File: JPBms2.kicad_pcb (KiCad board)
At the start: 4 copper layers, 69 x 39 mm, 134 parts, among them J1 XT30PW-M, J2 Conn_ARM_SWD_TagConnect_TC2030, Q1 AO3400A, Q10 2N7002, Q11 SK2301AW, Q12 SK2301AW, Q13 2N7002, Q14 SK2301AW, Q15 SK2301AW, Q16 2N7002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

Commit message: 94 unrouted
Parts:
- moved C7 10.3 mm to (125.6, 81.8), turned to -90 degrees
- moved R55 4.07 mm to (146.3, 71.4), turned to 180 degrees
- moved C22 4.07 mm to (129.0, 82.3), turned to -90 degrees
- moved R56 4.06 mm to (146.3, 75.4), turned to 180 degrees
- moved R4 3.51 mm to (124.1, 81.8), turned to 90 degrees
- moved R7 3.30 mm to (132.1, 82.3), turned to 90 degrees
- moved U1 3.07 mm to (147.8, 87.6), turned to 0 degrees
- moved D3 2.93 mm to (129.7, 79.0)
- moved R1 2.78 mm to (140.3, 78.5)
- moved C17 2.77 mm to (137.5, 78.2), turned to 90 degrees
- moved D18 2.54 mm to (132.3, 79.0)
- moved R32 2.42 mm to (138.8, 77.6), turned to 90 degrees
- moved C1 2.16 mm to (145.2, 87.7), turned to -90 degrees
- moved R36 2.09 mm to (140.2, 84.8)
- moved R37 1.99 mm to (140.2, 83.3)
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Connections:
- U3 pad 14: VBATT_ADC -> VSOLAR_ADC
- U3 pad 15: VSOLAR_ADC -> VBATT_ADC
- U3 pad 21: VBATT_ADC_EN -> CELL4V_ADC_EN
- U3 pad 23: CELL4V_ADC_EN -> VBATT_ADC_EN
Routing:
- net VDD: track 25.4 -> 76.6 mm, vias 0 -> 4
- net Net-(U1-OUT): track 0.00 -> 40.1 mm, vias 0 -> 2
- net /BuckBoost/DRIVER_VCC: track 9.47 -> 49.0 mm, vias 0 -> 2
- net CELL_8V: track 20.8 -> 59.7 mm, vias 0 -> 2
- net CELL_4V: track 23.4 -> 59.5 mm, vias 0 -> 2
- net Net-(Q12-D): track 0.00 -> 33.3 mm
- net VSOLAR: track 10.7 -> 34.6 mm
- net /MCU/USART1_RX: track 1.42 -> 18.0 mm
- net GND: track 9.99 -> 25.8 mm, vias 0 -> 15
- net +BATT: track 66.8 -> 79.2 mm
- net Net-(Q11-G): track 0.00 -> 12.0 mm
- net Net-(Q17-G): track 0.00 -> 10.5 mm
- net Net-(Q14-G): track 0.00 -> 10.5 mm
- net VBATT_ADC: track 2.80 -> 11.6 mm
- net /MCU/SWITCH: track 0.00 -> 8.33 mm
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- added copper zone on F.Cu, net /BuckBoost/VS_A

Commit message: 35 left
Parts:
- moved R36 11.3 mm to (129.2, 87.0), turned to 180 degrees
- moved R37 11.3 mm to (129.2, 85.5)
- moved C12 0.35 mm to (133.7, 73.2)
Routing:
- net GND: track 25.8 -> 92.0 mm, vias 15 -> 64
- net DD_TOP_B: track 0.00 -> 52.5 mm, vias 0 -> 2
- net DD_BOT_B: track 0.00 -> 49.6 mm, vias 0 -> 2
- net DD_TOP_A: track 0.00 -> 37.7 mm, vias 0 -> 2
- net /MCU/SWITCH: track 8.33 -> 45.4 mm, vias 0 -> 2
- net DD_BOT_A: track 0.00 -> 34.1 mm, vias 0 -> 2
- net /MCU/SWCLK: track 0.00 -> 31.7 mm, vias 0 -> 2
- net COMP2_INP: track 2.66 -> 32.4 mm, vias 0 -> 2
- net /MCU/SWDIO: track 0.00 -> 24.3 mm, vias 0 -> 2
- net VBATT_ADC_EN: track 0.00 -> 17.0 mm
- net VDD: track 76.6 -> 93.6 mm
- net CELL4V_ADC_EN: track 0.00 -> 11.8 mm, vias 0 -> 2
- net /MCU/NRST: track 2.19 -> 12.2 mm, vias 0 -> 1
- net /BuckBoost/VS_A: track 7.00 -> 16.0 mm
- net CELL8V_ADC_EN: track 0.00 -> 8.58 mm, vias 0 -> 2
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
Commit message: 17 left
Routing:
- net +BATT: track 79.2 -> 134.8 mm, vias 0 -> 3
- net NBAL_1: track 0.00 -> 36.6 mm, vias 0 -> 4
- net /MCU/LED_ERROR: track 0.00 -> 35.6 mm, vias 0 -> 2
- net /MCU/LED_ON: track 0.00 -> 35.2 mm
- net /MCU/LED_ACTIVE: track 0.00 -> 35.1 mm, vias 0 -> 2
- net DRIVERS_EN: track 2.08 -> 36.9 mm, vias 1 -> 2
- net /MCU/NRST: track 12.2 -> 38.0 mm, vias 1 -> 4
- net NBAL_2: track 0.00 -> 15.2 mm, vias 0 -> 3
- net Net-(Q17-D): track 0.00 -> 8.42 mm
- net Net-(Q14-D): track 0.00 -> 8.39 mm
- net Net-(Q11-D): track 0.00 -> 8.24 mm
- net NBAL_3: track 0.00 -> 8.13 mm, vias 0 -> 2
- net GND: track 92.0 -> 96.6 mm, vias 64 -> 74
- net /BuckBoost/VS_A: track 16.0 -> 19.5 mm
- net DD_BOT_A: track 34.1 -> 35.9 mm
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
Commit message: It is routed
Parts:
- turned D11 to 180 degrees
- turned D12 to 180 degrees
- turned D13 to 180 degrees
- turned R43 to 180 degrees
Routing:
- net Net-(D11-A): track 4.87 -> 25.9 mm, vias 0 -> 2
- net Net-(D12-A): track 4.17 -> 22.8 mm, vias 0 -> 2
- net CELL_8V: track 59.8 -> 73.1 mm, vias 2 -> 4
- net Net-(D13-A): track 4.79 -> 17.2 mm, vias 0 -> 2
- net CELL_4V: track 60.5 -> 70.4 mm, vias 2 -> 4
- net Net-(U1-OUT): track 40.1 -> 48.1 mm, vias 2 -> 4
- net GND: track 96.6 -> 104.2 mm, vias 74 -> 112
- net Net-(D12-K): track 0.00 -> 1.24 mm
- net Net-(D13-K): track 0.00 -> 1.24 mm
- net DD_BOT_B: track 49.8 -> 51.0 mm
- net Net-(D11-K): track 0.00 -> 1.24 mm
- net Net-(U4-LVG): track 9.50 -> 8.64 mm
- net /MCU/LED_ERROR: track 35.6 -> 36.4 mm
- net +BATT: track 134.8 -> 133.9 mm
- net NBAL_2: track 15.2 -> 14.9 mm, vias 3 -> 2

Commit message: Fine tuning routing
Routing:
- net /MCU/SWITCH: track 45.7 -> 48.6 mm
- net VBATT_ADC_EN: track 17.0 -> 19.3 mm
- net /BuckBoost/DRIVER_VCC: track 50.0 -> 51.7 mm
- net DD_BOT_B: track 51.0 -> 49.8 mm
- net DD_TOP_B: track 53.1 -> 53.8 mm
- net GND: vias 112 -> 113
- net /BuckBoost/VS_B: vias 0 -> 11
- net /BuckBoost/VS_A: vias 0 -> 9
- added copper zone on F.Cu, net +BATT
- added copper zone on B.Cu, net /BuckBoost/VS_A
- added copper zone on B.Cu, net /BuckBoost/VS_B
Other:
- board text added: "V1.2 X Move solar adc line to other layer for less noise? X Move adc sampling capacitors closest to stm32 X stm power pins should be wired to capacitors, then those wired to vcc/gnd - multiple gnd vias around decoupling caps X balance resistors are placed in a weird grouping X bootstrap diodes backwards X Check, do I need vcc for level shifting on the BMP uart? X Could I make the uart only turn o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"
- board text removed: "V1.2 - Move solar adc line to other layer for less noise? - Move adc sampling capacitors closest to stm32 - stm power pins should be wired to capacitors, then those wired to vcc/gnd - multiple gnd vias around decoupling caps X balance resistors are placed in a weird grouping X bootstrap diodes backwards X Check, do I need vcc for level shifting on the BMP uart? X Could I make the uart only turn o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"

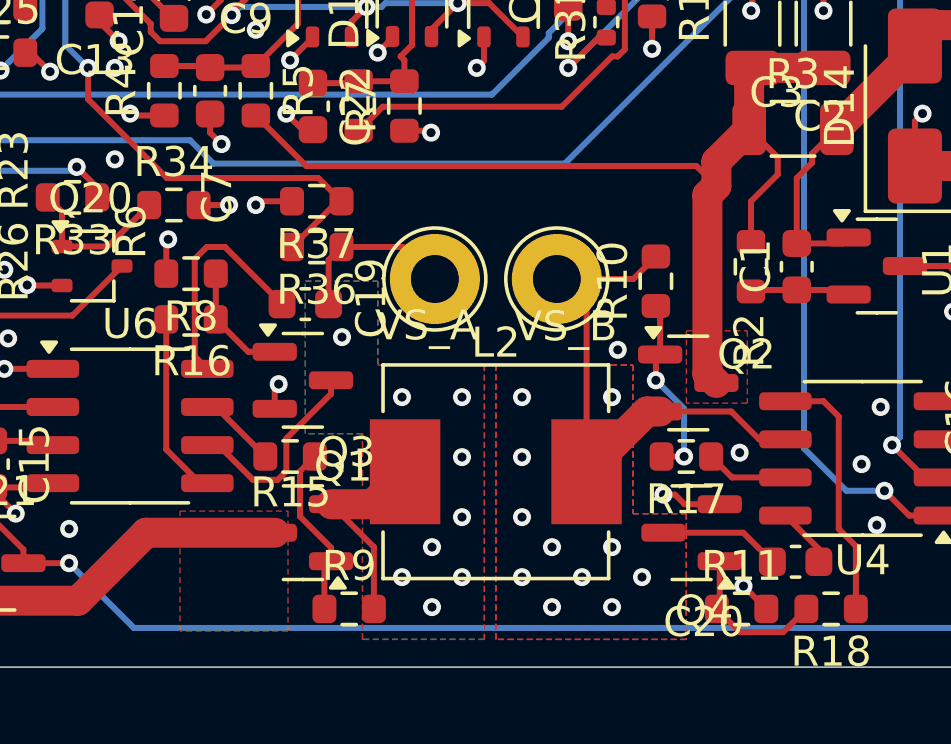
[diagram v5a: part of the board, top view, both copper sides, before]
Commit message: Better thermal pads
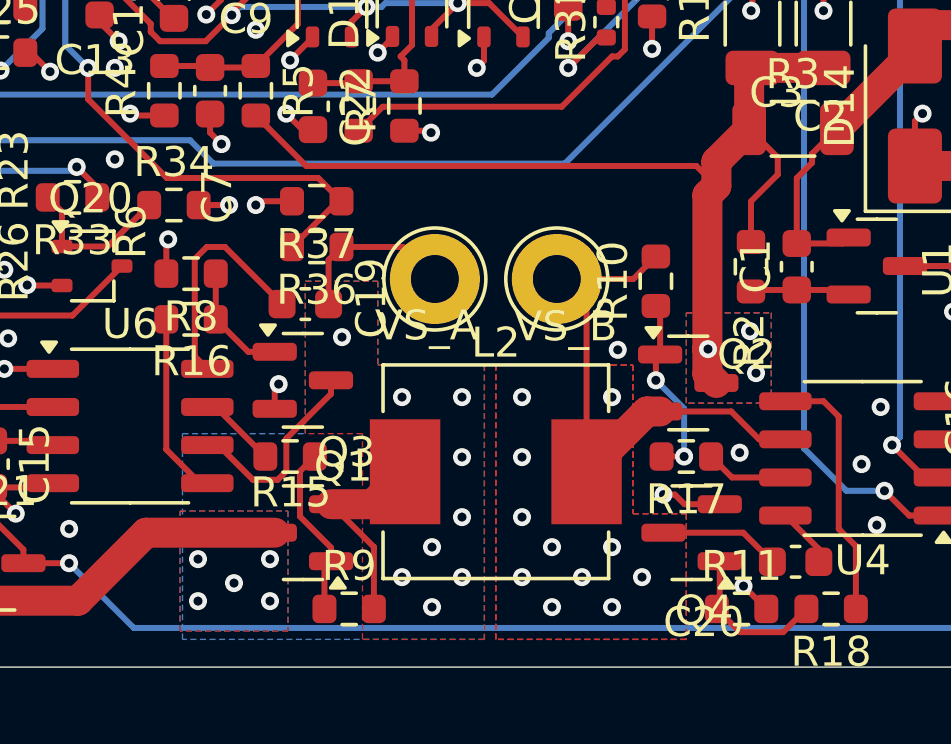
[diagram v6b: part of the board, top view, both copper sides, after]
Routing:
- net VSOLAR: vias 0 -> 3
- net +BATT: vias 3 -> 8
- added copper zone on B.Cu, net +BATT
- added copper zone on B.Cu, net VSOLAR
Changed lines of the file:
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@@
 	)
 	(via
+		(at 127.6 97.4)
+		(size 0.6)
+		(drill 0.3)
+		(layers "F.Cu" "B.Cu")
+		(free yes)
+		(net 7)
+	)
+	(via
+		(at 127.6 98.8)
+		(size 0.6)
+		(drill 0.3)
+		(layers "F.Cu" "B.Cu")
+		(free yes)
+		(net 7)
+	)
+	(via
+		(at 125.2 97.4)
+		(size 0.6)
+		(drill 0.3)
+		(layers "F.Cu" "B.Cu")
+		(free yes)
+		(net 7)
+	)
+	(via
 		(at 143.764 67.564)
 		(size 0.6)
@@
 	)
 	(via
+		(at 125.2 98.8)
+		(size 0.6)
+		(drill 0.3)
+		(layers "F.Cu" "B.Cu")
+		(free yes)
+		(net 7)
+	)
+	(via
 		(at 139.806555 63.388)
 		(size 0.6)
@@
 	)
 	(via
+		(at 126.4 98.2)
+		(size 0.6)
+		(drill 0.3)
+		(layers "F.Cu" "B.Cu")
+		(free yes)
+		(net 7)
+	)
+	(via
 		(at 140.399002 67.499998)
 		(size 0.6)
@@
 	)
 	(segment
+		(start 142.2 90.4)
+		(end 142.179652 90.379652)
+		(width 1)
+		(layer "F.Cu")
+		(net 13)
+	)
+	(segment
+		(start 142.179652 90.420348)
+		(end 142.2 90.4)
+		(width 1)
+		(layer "F.Cu")
+		(net 13)
+	)
+	(segment
 		(start 144.526 84.582)
 		(end 143.632783 85.475217)
@@
 	)
 	(segment
-		(start 142.179652 91.229351)
+		(start 142.179652 90.379652)
 		(end 142.179652 85.262999)
 		(width 1)
@@
 	)
 	(segment
+		(start 142.179652 91.229351)
+		(end 142.179652 90.420348)
+		(width 1)
+		(layer "F.Cu")
+		(net 13)
+	)
+	(segment
 		(start 142.479651 91.52935)
 		(end 142.179652 91.229351)
@@
 		(net 13)
 	)
+	(via
+		(at 143.8 91.2)
+		(size 0.6)
+		(drill 0.3)
+		(layers "F.Cu" "B.Cu")
+		(free yes)
+		(net 13)
+	)
+	(via
+		(at 142.2 90.4)
+		(size 0.6)
+		(drill 0.3)
+		(layers "F.Cu" "B.Cu")
+		(net 13)
+	)
+	(via
+		(at 143.6 89.8)
+		(size 0.6)
+		(drill 0.3)
+		(layers "F.Cu" "B.Cu")
+		(free yes)
+		(net 13)
+	)
 	(segment
 		(start 122.750924 70.07)
@@
 	)
 	(zone
-		(net 13)
-		(net_name "VSOLAR")
+		(net 22)
+		(net_name "/BuckBoost/VS_B")
 		(layer "F.Cu")
 		(hatch edge 0.5)
-		(priority 2)
+		(priority 3)
 		(connect_pads yes
 			(clearance 0.2)
@@
 		(polygon
 			(pts
-				(xy 141.478 89.789) (xy 143.51 89.789) (xy 143.51 92.202) (xy 141.478 92.202)
+				(xy 135.128 90.932) (xy 139.7 90.932) (xy 139.7 95.885) (xy 141.478 95.885) (xy 141.478 100.076)
+				(xy 135.128 100.076)
 			)
 		)
 	)
 	(zone
-		(net 22)
-		(net_name "/BuckBoost/VS_B")
+		(net 20)
+		(net_name "/BuckBoost/VS_A")
 		(layer "F.Cu")
 		(hatch edge 0.5)
-		(priority 3)
+		(priority 4)
 		(connect_pads yes
 			(clearance 0.2)
@@
 		(polygon
 			(pts
-				(xy 135.128 90.932) (xy 139.7 90.932) (xy 139.7 95.885) (xy 141.478 95.885) (xy 141.478 100.076)
-				(xy 135.128 100.076)
+				(xy 128.778 88.138) (xy 131.191 88.138) (xy 131.191 90.932) (xy 134.747 90.932) (xy 134.747 100.076)
+				(xy 130.683 100.076) (xy 130.683 93.218) (xy 128.778 93.218)
 			)
 		)
 	)
 	(zone
-		(net 7)
-		(net_name "+BATT")
-		(layer "F.Cu")
+		(net 13)
+		(net_name "VSOLAR")
+		(layers "F&B.Cu")
 		(hatch edge 0.5)
-		(priority 5)
+		(priority 2)
 		(connect_pads yes
 			(clearance 0.2)
@@
 			(thermal_gap 0.5)
 			(thermal_bridge_width 0.5)
+			(island_removal_mode 1)
+			(island_area_min 10)
 		)
 		(polygon
 			(pts
-				(xy 124.6 95.8) (xy 128.2 95.8) (xy 128.2 99.8) (xy 124.6 99.8)
+				(xy 141.478 89.189) (xy 144.31 89.189) (xy 144.31 92.202) (xy 141.478 92.202)
 			)
 		)
 	)
 	(zone
-		(net 20)
-		(net_name "/BuckBoost/VS_A")
-		(layer "F.Cu")
+		(net 7)
+		(net_name "+BATT")
+		(layers "F&B.Cu")
 		(hatch edge 0.5)
-		(priority 4)
+		(priority 5)
 		(connect_pads yes
 			(clearance 0.2)
@@
 			(thermal_gap 0.5)
 			(thermal_bridge_width 0.5)
+			(island_removal_mode 1)
+			(island_area_min 10)
 		)
 		(polygon
 			(pts
-				(xy 128.778 88.138) (xy 131.191 88.138) (xy 131.191 90.932) (xy 134.747 90.932) (xy 134.747 100.076)
-				(xy 130.683 100.076) (xy 130.683 93.218) (xy 128.778 93.218)
+				(xy 124.6 95.8) (xy 128.2 95.8) (xy 128.2 99.8) (xy 124.6 99.8)
 			)
 		)
@@
 			(pts
 				(xy 128.778 88.138) (xy 131.191 88.138) (xy 131.191 90.932) (xy 134.747 90.932) (xy 134.747 100.076)
-				(xy 130.683 100.076) (xy 130.683 93.218) (xy 128.778 93.218)
+				(xy 124.683 100.076) (xy 124.683 93.218) (xy 128.778 93.218)
 			)
 		)

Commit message: Starting cleanup
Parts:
- renumbered L2 to L1
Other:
- board text removed: "2.5V"
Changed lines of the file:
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@@
 		(tags "SO SO")
 		(property "Reference" "U4"
-			(at 0 -3.4 180)
+			(at -4.645 -2.157 180)
 			(layer "F.SilkS")
 			(effects
@@
 		(tags "resistor")
 		(property "Reference" "R9"
-			(at 0 -1.43 0)
+			(at 0 1.34 0)
 			(layer "F.SilkS")
 			(effects
@@
 		(tags "capacitor")
 		(property "Reference" "C19"
-			(at -2.2 0.2 -90)
+			(at -2.022 0.1 -90)
 			(layer "F.SilkS")
 			(effects
@@
 		(tags "LED")
 		(property "Reference" "D12"
-			(at 0 -1.43 180)
+			(at -5.2025 -0.118 180)
 			(layer "F.SilkS")
 			(effects
@@
 		(tags "SOT TO_SOT_SMD")
 		(property "Reference" "U1"
-			(at 2.044175 0.125049 90)
+			(at -0.028 2.37 180)
 			(layer "F.SilkS")
 			(effects
@@
 		(descr "Inductor, Sunlord, MWSA0605S, 7.0x6.6x4.8mm, https://sunlordinc.com/Download.aspx?file=L1VwbG9hZEZpbGVzL1BERl9DYXQvMjAyMjExMTUxNDQ4MDU0NTQucGRm&lan=en")
 		(tags "Inductor mwsa")
-		(property "Reference" "L2"
+		(property "Reference" "L1"
 			(at 0 -4.3 0)
 			(layer "F.SilkS")
@@
 		(tags "fuse")
 		(property "Reference" "F2"
-			(at -3.38 0.28 0)
+			(at 2.911504 0.044 0)
 			(layer "F.SilkS")
 			(effects
@@
 		(tags "resistor")
 		(property "Reference" "R36"
-			(at 0 -1.43 180)
+			(at 2.159 -0.005 -90)
 			(layer "F.SilkS")
 			(effects
@@
 		(tags "capacitor")
 		(property "Reference" "C4"
-			(at 2.75 -0.5 0)
+			(at 1.482 -2.088 0)
 			(layer "F.SilkS")
 			(effects
@@
 		(tags "resistor")
 		(property "Reference" "R15"
-			(at 0.025 1.2 0)
+			(at 1.93 -0.18 90)
 			(layer "F.SilkS")
 			(effects
@@
 			(at 0 -1.17 180)
 			(layer "F.SilkS")
+			(hide yes)
 			(effects
 				(font
@@
 		(tags "capacitor")
 		(property "Reference" "C1"
-			(at -0.017643 1.362286 90)
+			(at -2.453547 -0.041275 90)
 			(layer "F.SilkS")
 			(effects
@@
 		(tags "tag connect programming header pogo pins")
 		(property "Reference" "J2"
-			(at -4.99 2.585 180)
+			(at 0.01 4.485 180)
 			(layer "F.SilkS")
 			(effects
@@
 			(at -0.05 1.8 180)
 			(layer "F.SilkS")
+			(hide yes)
 			(effects
 				(font
@@
 		(tags "resistor")
 		(property "Reference" "R18"
-			(at 0 -1.43 180)
+			(at 0 -1.54 180)
 			(layer "F.SilkS")
 			(effects
@@
 		(tags "Diode SOD882 DFN1006-2")
 		(property "Reference" "D15"
-			(at 0.15 1.8 180)
+			(at 0.834 -2.201864 180)
 			(layer "F.SilkS")
+			(hide yes)
 			(effects
 				(font
@@
 			(at 0 -1.17 180)
 			(layer "F.SilkS")
+			(hide yes)
 			(effects
 				(font
@@
 		(tags "LED")
 		(property "Reference" "D13"
-			(at 0 -1.43 180)
+			(at -5.2025 0.006 180)
 			(layer "F.SilkS")
 			(effects
@@
 			(at -0.05 1.8 180)
 			(layer "F.SilkS")
+			(hide yes)
 			(effects
 				(font
@@
 			(at 0 -1.17 180)
 			(layer "F.SilkS")
+			(hide yes)
 			(effects
 				(font
@@
 		(tags "LED")
 		(property "Reference" "D11"
-			(at 0 -1.43 180)
+			(at -5.2025 -0.042 180)
 			(layer "F.SilkS")
 			(effects
@@
 		(tags "connector Molex PicoBlade side entry")
 		(property "Reference" "UART1"
-			(at 2.968 4.211 0)
+			(at 0.348 -2.436 0)
 			(layer "F.SilkS")
 			(effects
@@
 		(tags "capacitor")
 		(property "Reference" "C11"
-			(at 2.66 0.22 90)
+			(at 2.86 -0.08 90)
 			(layer "F.SilkS")
 			(effects
@@
 		(tags "resistor")
 		(property "Reference" "R37"
-			(at 0 -1.43 180)
+			(at -0.041 1.071 0)
 			(layer "F.SilkS")
 			(effects
@@
 		(tags "capacitor")
 		(property "Reference" "C5"
-			(at 2.848852 0.865192 0)
+			(at 2.848852 -0.138 0)
 			(layer "F.SilkS")
 			(effects
@@
 		(tags "resistor")
 		(property "Reference" "R2"
-			(at 2.455 0.0485 90)
+			(at -2.453547 0.032783 90)
 			(layer "F.SilkS")
 			(effects
@@
 		(tags "capacitor")
 		(property "Reference" "C16"
-			(at -0.025 1.25 90)
+			(at -0.025 -1.508 90)
 			(layer "F.SilkS")
 			(effects
@@
 		(tags "capacitor")
 		(property "Reference" "C20"
-			(at -3.063 2.013 0)
+			(at 2.879475 -0.088936 0)
 			(layer "F.SilkS")
 			(effects
@@
 		(tags "fuse")
 		(property "Reference" "F1"
-			(at -3.28 0.08 0)
+			(at 2.898 0.104 0)
 			(layer "F.SilkS")
 			(effects
@@
 		(tags "capacitor")
 		(property "Reference" "C21"
-			(at 0 1.4 90)
+			(at -1.989125 0.195515 180)
 			(layer "F.SilkS")
 			(effects
@@
 		(tags "Diode SOD882 DFN1006-2")
 		(property "Reference" "D7"
-			(at 0 -1.35 90)
+			(at -0.262 1.456 90)
 			(layer "F.SilkS")
 			(effects
@@
 		(tags "resistor")
 		(property "Reference" "R10"
-			(at 0 -1.43 -90)
+			(at 0 1.338 -90)
 			(layer "F.SilkS")
 			(effects
@@
 		(tags "SOT TO_SOT_SMD")
 		(property "Reference" "Q4"
-			(at -0.4135 -2.6 180)
+			(at 0.8535 -2.48 180)
 			(layer "F.SilkS")
 			(effects
@@
 		(tags "SOT TO_SOT_SMD")
 		(property "Reference" "Q1"
-			(at -1.3375 2.2 180)
+			(at 0.8995 -2.48 0)
 			(layer "F.SilkS")
 			(effects
@@
 		(tags "SOT TO_SOT_SMD")
 		(property "Reference" "Q3"
-			(at 1.445 2.4 0)
+			(at 2.905 -1.24 0)
 			(layer "F.SilkS")
 			(effects
@@
 		(tags "fuse")
 		(property "Reference" "F3"
-			(at -3.38 0.28 0)
+			(at 2.898 -0.016 0)
 			(layer "F.SilkS")
 			(effects
@@
 		(tags "SO SO")
 		(property "Reference" "U6"
-			(at 0 -3.4 0)
+			(at -1.136 -3.364 0)
 			(layer "F.SilkS")
 			(effects
@@
 		(tags "Diode SOD882 DFN1006-2")
 		(property "Reference" "D8"
-			(at 0 -1.35 90)
+			(at 1.96 -0.144 90)
 			(layer "F.SilkS")
 			(effects
@@
 		(tags "resistor")
 		(property "Reference" "R11"
-			(at 0 -1.43 0)
+			(at 0 1.54 0)
 			(layer "F.SilkS")
 			(effects
@@
 		(tags "resistor")
 		(property "Reference" "R17"
-			(at 0 -1.43 180)
+			(at -1.922 -0.02 90)
 			(layer "F.SilkS")
 			(effects
@@
 		(tags "SOT TO_SOT_SMD")
 		(property "Reference" "Q2"
-			(at 1.9375 -0.946 0)
+			(at 3.057849 -0.92935 0)
 			(layer "F.SilkS")
 			(effects
@@
 		)
 	)
-	(gr_text "2.5V"
-		(at 113.2 65.4 0)
-		(layer "F.SilkS")
-		(effects
-			(font
-				(size 1 1)
-				(thickness 0.1)
-			)
-			(justify left bottom)
-		)
-	)
 	(gr_text "GND"
-		(at 99.314 72.644 0)
+		(at 100.4 91 0)
 		(layer "F.SilkS")
 		(effects
@@
 	)
 	(gr_text "+BATT"
-		(at 101.4 91.4 0)
+		(at 105 75.6 0)
 		(layer "F.SilkS")
 		(effects
@@
 	)
 	(gr_text "VS_A"
-		(at 131.095 90.198 0)
+		(at 131 86 0)
 		(layer "F.SilkS")
 		(effects
@@
 	)
 	(gr_text "VS_B"
-		(at 135.74 90.228 0)
+		(at 135.6 86 0)
 		(layer "F.SilkS")
 		(effects

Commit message: Some label cleanup, but it's a packed board
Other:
- board text added: "ACT"
- board text added: "BAL1 BAL2 BAL3"
- board text added: "ERR"
- board text added: "ON"
